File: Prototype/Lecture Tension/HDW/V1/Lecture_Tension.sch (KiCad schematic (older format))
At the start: 34 parts

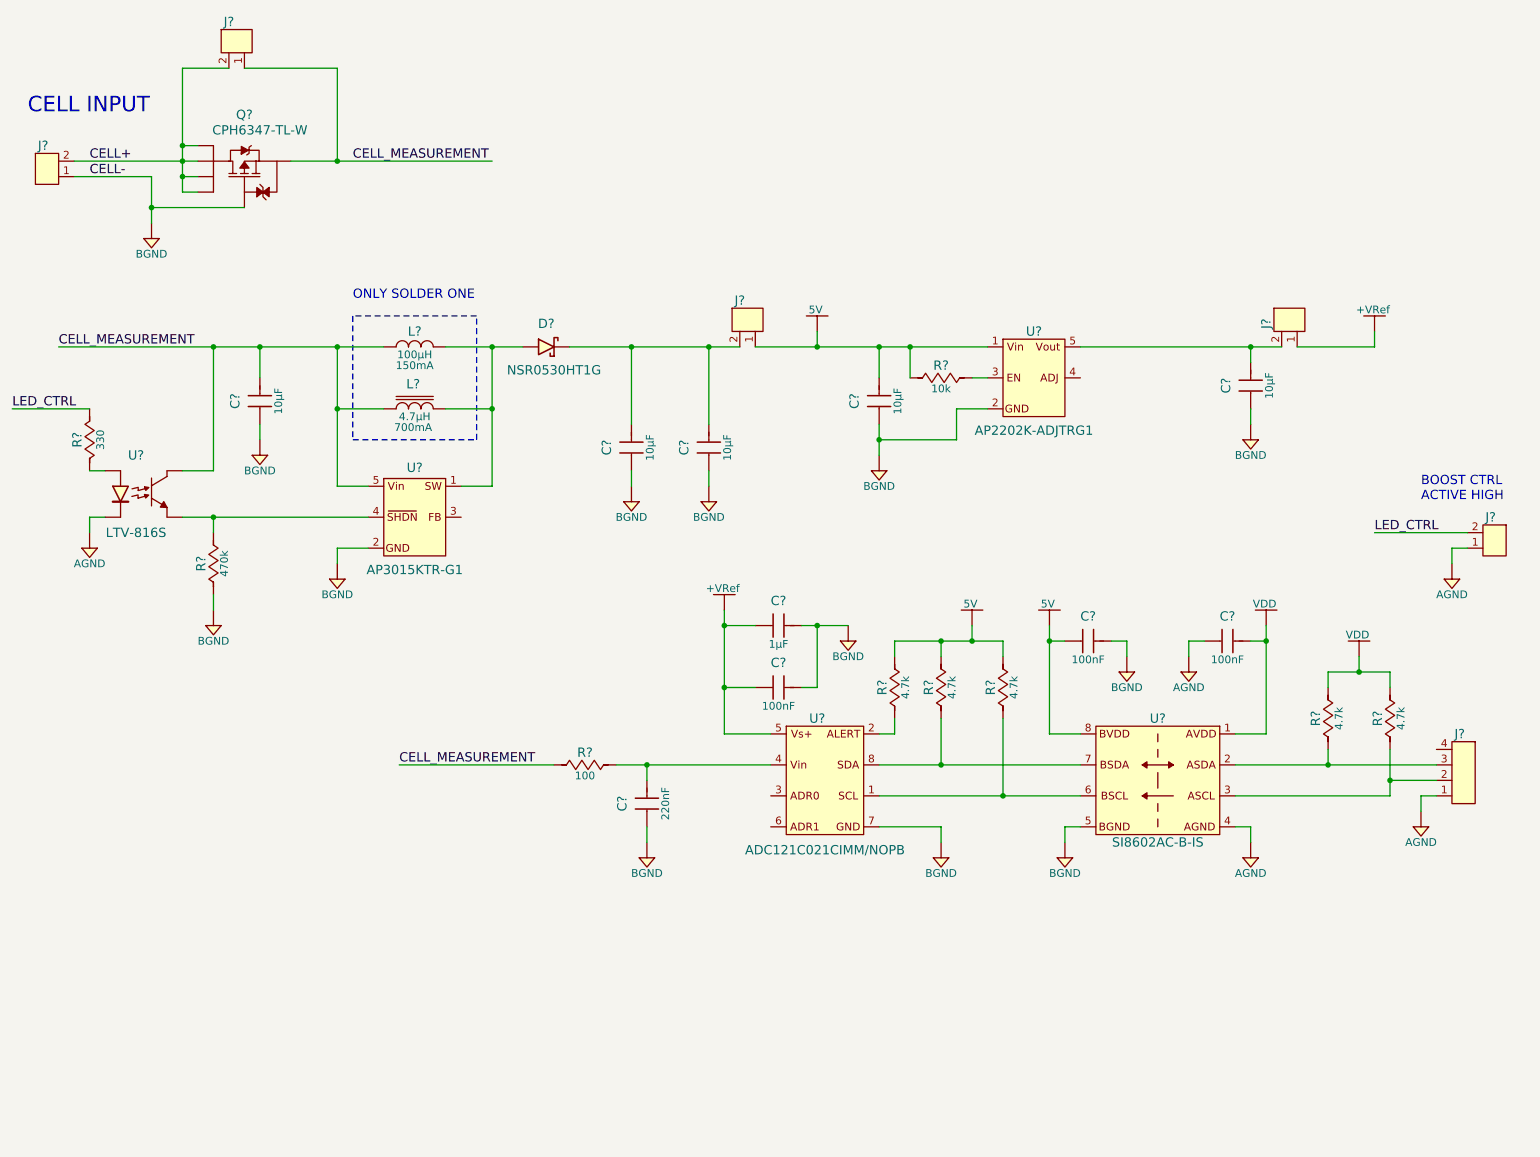
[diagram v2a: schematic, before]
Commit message: need tension divider LDO
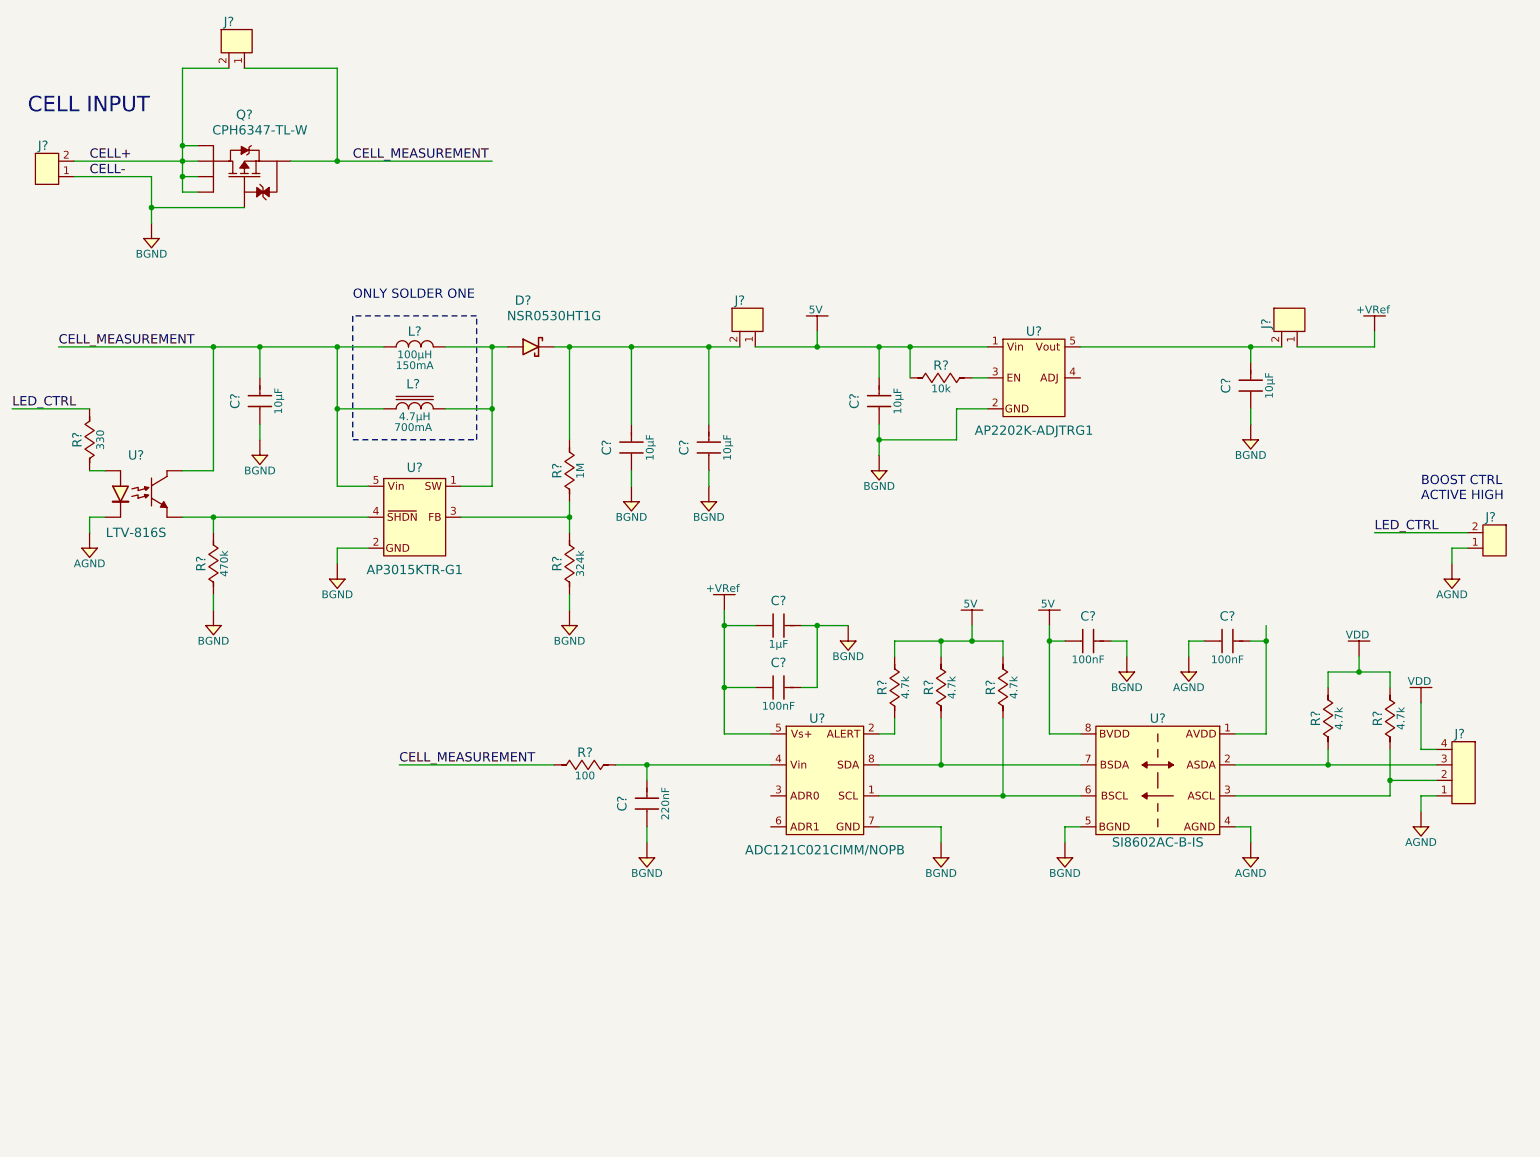
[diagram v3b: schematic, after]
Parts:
- added R?: RC0805JR-071ML, Resistors:R0805, symbol RC0805JR-071ML
- added R?: RC0805FR-07324KL, Resistors:R0805, symbol RC0805FR-07324KL
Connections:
- net BGND: now also R?.1
- net VDD: now also J?.4; no longer C?.2, U?.1 (AVDD)
- net at U?.3 (FB): now also R?.1, R?.2
- net at C?.2, C?.2, D?.1 (Cathode)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: now also R?.2
- new net: C?.2, U?.1 (AVDD)
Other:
- moved on the sheet: D?
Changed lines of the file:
@@
 L VDD #PWR?
 U 1 1 591B5717
-P 8700 4500
-F 0 "#PWR?" H 8700 4350 50  0001 C CNN
-F 1 "VDD" H 8690 4640 50  0000 C CNN
-F 2 "" H 8700 4500 60  0000 C CNN
-F 3 "" H 8700 4350 60  0000 C CNN
-	1    8700 4500
+P 9700 5000
+F 0 "#PWR?" H 9700 4850 50  0001 C CNN
+F 1 "VDD" H 9690 5140 50  0000 C CNN
+F 2 "" H 9700 5000 60  0000 C CNN
+F 3 "" H 9700 4850 60  0000 C CNN
+	1    9700 5000
 	1    0    0    -1
 $EndComp
@@
 	8600 4600 8700 4600
 Wire Wire Line
-	8700 4500 8700 4600
-Wire Wire Line
-	8700 4600 8700 5200
+	8700 4500 8700 5200
 Wire Wire Line
 	8200 4700 8200 4600
@@
 	9100 4900 9100 4800
 Wire Wire Line
-	9100 4800 9300 4800
-Wire Wire Line
-	9300 4800 9500 4800
+	9100 4800 9500 4800
 Wire Wire Line
 	9300 4800 9300 4700
 Connection ~ 9300 4800
 Wire Wire Line
-	8500 5400 9100 5400
-Wire Wire Line
-	9100 5400 9800 5400
+	8500 5400 9800 5400
 Wire Wire Line
 	9100 5400 9100 5300
@@
 	9500 4800 9500 4900
 Wire Wire Line
-	9500 5300 9500 5500
-Wire Wire Line
-	9500 5500 9500 5600
+	9500 5300 9500 5600
 Wire Wire Line
 	9500 5600 8500 5600
@@
 $EndComp
 Wire Wire Line
-	7300 4500 7300 4600
-Wire Wire Line
-	7300 4600 7300 5200
+	7300 4500 7300 5200
 Wire Wire Line
 	7300 4600 7400 4600
@@
 $EndComp
 Wire Wire Line
-	5200 4400 5200 4500
-Wire Wire Line
-	5200 4500 5200 4900
-Wire Wire Line
-	5200 4900 5200 5200
+	5200 4400 5200 5200
 Wire Wire Line
 	5200 5200 5500 5200
@@
 	5800 4900 5800 4500
 Wire Wire Line
-	5700 4500 5800 4500
-Wire Wire Line
-	5800 4500 6000 4500
+	5700 4500 6000 4500
 Connection ~ 5800 4500
 $Comp
@@
 	6600 4700 6600 4600
 Wire Wire Line
-	6300 4600 6600 4600
-Wire Wire Line
-	6600 4600 6800 4600
-Wire Wire Line
-	6800 4600 7000 4600
+	6300 4600 7000 4600
 Wire Wire Line
 	7000 4600 7000 4700
@@
 Connection ~ 6800 4600
 Wire Wire Line
-	6200 5400 6600 5400
-Wire Wire Line
-	6600 5400 7500 5400
+	6200 5400 7500 5400
 Wire Wire Line
 	6600 5400 6600 5100
@@
 	7000 5100 7000 5600
 Wire Wire Line
-	6200 5600 7000 5600
-Wire Wire Line
-	7000 5600 7500 5600
+	6200 5600 7500 5600
 Connection ~ 7000 5600
 $Comp
@@
 $EndComp
 Wire Wire Line
-	1000 1500 1700 1500
-Wire Wire Line
-	1700 1500 1800 1500
+	1000 1500 1800 1500
 Wire Wire Line
 	1000 1600 1500 1600
@@
 $EndComp
 Wire Wire Line
-	1500 1600 1500 1800
-Wire Wire Line
-	1500 1800 1500 1900
-Wire Wire Line
-	1700 900  1700 1400
-Wire Wire Line
-	1700 1400 1700 1500
-Wire Wire Line
-	1700 1500 1700 1600
-Wire Wire Line
-	1700 1600 1700 1700
+	1500 1600 1500 1900
+Wire Wire Line
+	1700 900  1700 1700
 Wire Wire Line
 	1700 1400 1800 1400
@@
 	2700 900  2700 1500
 Wire Wire Line
-	2400 1500 2700 1500
-Wire Wire Line
-	2700 1500 3700 1500
+	2400 1500 3700 1500
 Text Label 2800 1500 0    60   ~ 0
 CELL_MEASUREMENT
@@
 CELL_MEASUREMENT
 Wire Wire Line
-	4500 5400 4700 5400
-Wire Wire Line
-	4700 5400 5500 5400
+	4500 5400 5500 5400
 Wire Wire Line
 	4700 5500 4700 5400
@@
 	3000 3100 2700 3100
 Wire Wire Line
-	2700 2700 2700 3100
-Wire Wire Line
-	2700 3100 2700 3600
+	2700 2700 2700 3600
 Wire Wire Line
 	2700 3600 2900 3600
 Wire Wire Line
-	900  2700 1900 2700
-Wire Wire Line
-	1900 2700 2200 2700
-Wire Wire Line
-	2200 2700 2700 2700
-Wire Wire Line
-	2700 2700 3000 2700
+	900  2700 3000 2700
 Connection ~ 2700 3100
 Wire Wire Line
-	3400 2700 3700 2700
-Wire Wire Line
-	3700 2700 3900 2700
-Wire Wire Line
-	3700 2700 3700 3100
-Wire Wire Line
-	3700 3100 3700 3600
+	3400 2700 3800 2700
+Wire Wire Line
+	3700 2700 3700 3600
 Wire Wire Line
 	3700 3600 3500 3600
@@
 	1100 3800 1100 3900
 Wire Wire Line
-	1700 3800 1900 3800
-Wire Wire Line
-	1900 3800 2900 3800
+	1700 3800 2900 3800
 Text Label 900  2700 0    60   ~ 0
 CELL_MEASUREMENT
@@
 L NSR0530HT1G D?
 U 1 1 591BD4B8
-P 4100 2700
-F 0 "D?" H 4050 2850 60  0000 C CNN
-F 1 "NSR0530HT1G" H 4100 2550 60  0000 C CNN
-F 2 "Diodes:SOD-323" H 4080 1700 60  0001 C CNN
-F 3 "http://www.onsemi.com/pub/Collateral/NSR0530H-D.PDF" H 4080 1600 60  0001 C CNN
-F 4 "Digikey" H 4080 2200 60  0001 C CNN "Supplier"
-F 5 "NSR0530HT1GOSCT-ND" H 4080 2100 60  0001 C CNN "Supplier Part Number"
-F 6 "ON Semiconductor" H 4080 2000 60  0001 C CNN "Manufacturer"
-F 7 "NSR0530HT1G" H 4080 1900 60  0001 C CNN "Manufacturer Part Number"
-F 8 "DIODE SCHOTTKY 30V 500MA SOD323" H 4080 1800 60  0001 C CNN "Description"
-	1    4100 2700
+P 4000 2700
+F 0 "D?" H 3900 3000 60  0000 C CNN
+F 1 "NSR0530HT1G" H 4100 2900 60  0000 C CNN
+F 2 "Diodes:SOD-323" H 3980 1700 60  0001 C CNN
+F 3 "http://www.onsemi.com/pub/Collateral/NSR0530H-D.PDF" H 3980 1600 60  0001 C CNN
+F 4 "Digikey" H 3980 2200 60  0001 C CNN "Supplier"
+F 5 "NSR0530HT1GOSCT-ND" H 3980 2100 60  0001 C CNN "Supplier Part Number"
+F 6 "ON Semiconductor" H 3980 2000 60  0001 C CNN "Manufacturer"
+F 7 "NSR0530HT1G" H 3980 1900 60  0001 C CNN "Manufacturer Part Number"
+F 8 "DIODE SCHOTTKY 30V 500MA SOD323" H 3980 1800 60  0001 C CNN "Description"
+	1    4000 2700
 	1    0    0    -1
 $EndComp
 Connection ~ 3700 2700
 Wire Wire Line
-	4200 2700 4600 2700
-Wire Wire Line
-	4600 2700 5100 2700
-Wire Wire Line
-	5100 2700 5300 2700
+	4100 2700 5300 2700
 $Comp
 L 885012107014 C?
@@
 	5800 2600 5800 2700
 Wire Wire Line
-	5400 2700 5800 2700
-Wire Wire Line
-	5800 2700 6200 2700
-Wire Wire Line
-	6200 2700 6400 2700
-Wire Wire Line
-	6400 2700 6900 2700
+	5400 2700 6900 2700
 $Comp
 L 885012107014 C?
@@
 $EndComp
 Wire Wire Line
-	6200 3200 6200 3300
-Wire Wire Line
-	6200 3300 6200 3400
+	6200 3200 6200 3400
 Wire Wire Line
 	6900 3100 6700 3100
@@
 $EndComp
 Wire Wire Line
-	7500 2700 8600 2700
-Wire Wire Line
-	8600 2700 8800 2700
+	7500 2700 8800 2700
 Wire Wire Line
 	8600 2700 8600 2800
@@
 	0    -1   1    0
 $EndComp
+$Comp
+L RC0805JR-071ML R?
+U 1 1 591C2F0F
+P 4200 3500
+F 0 "R?" H 4200 3580 60  0000 C CNN
+F 1 "RC0805JR-071ML" H 4200 3200 50  0001 C CNN
+F 2 "Resistors:R0805" H 4200 2600 30  0001 C CNN
+F 3 "http://www.yageo.com/documents/recent/PYu-RC_Group_51_RoHS_L_7.pdf" H 4200 2550 30  0001 C CNN
+F 4 "Digikey" H 4200 3100 60  0001 C CNN "Supplier"
+F 5 "311-1.0MARCT-ND" H 4200 3000 60  0001 C CNN "Supplier Part Number"
+F 6 "Yageo" H 4200 2900 60  0001 C CNN "Manufacturer"
+F 7 "RC0805JR-071ML" H 4200 2800 60  0001 C CNN "Manufacturer Part Number"
+F 8 "RES SMD 1M OHM 5% 1/8W 0805" H 4200 2700 60  0001 C CNN "Description"
+F 9 "1M" H 4200 3430 50  0000 C CNN "Resistance (Ohms)"
+F 10 "±5%" H 4610 3420 50  0001 C CNN "Tolerance (%)"
+F 11 "1/8W" H 4200 3360 50  0001 C CNN "Puissance (Watts)"
+	1    4200 3500
+	0    -1   -1   0
+$EndComp
+Wire Wire Line
+	4200 3300 4200 2700
+Connection ~ 4200 2700
+Wire Wire Line
+	4200 3700 4200 3900
+Wire Wire Line
+	4200 3800 3500 3800
+$Comp
+L RC0805FR-07324KL R?
+U 1 1 591C3C0D
+P 4200 4100
+F 0 "R?" H 4200 4180 60  0000 C CNN
+F 1 "RC0805FR-07324KL" H 4200 3800 50  0001 C CNN
+F 2 "Resistors:R0805" H 4200 3200 30  0001 C CNN
+F 3 "http://www.yageo.com/documents/recent/PYu-RC_Group_51_RoHS_L_7.pdf" H 4200 3150 30  0001 C CNN
+F 4 "Digikey" H 4200 3700 60  0001 C CNN "Supplier"
+F 5 "311-324KCRCT-ND" H 4200 3600 60  0001 C CNN "Supplier Part Number"
+F 6 "Yageo" H 4200 3500 60  0001 C CNN "Manufacturer"
+F 7 "RC0805FR-07324KL" H 4200 3400 60  0001 C CNN "Manufacturer Part Number"
+F 8 "RES SMD 324K OHM 1% 1/8W 0805" H 4200 3300 60  0001 C CNN "Description"
+F 9 "324k" H 4200 4030 50  0000 C CNN "Resistance (Ohms)"
+F 10 "±1%" H 4610 4020 50  0001 C CNN "Tolerance (%)"
+F 11 "1/8W" H 4200 3960 50  0001 C CNN "Puissance (Watts)"
+	1    4200 4100
+	0    -1   -1   0
+$EndComp
+$Comp
+L BGND #PWR?
+U 1 1 591C3CA2
+P 4200 4500
+F 0 "#PWR?" H 4200 4330 50  0001 C CNN
+F 1 "BGND" H 4200 4400 50  0000 C CNN
+F 2 "" H 4200 4600 60  0000 C CNN
+F 3 "" H 4180 4410 60  0000 C CNN
+	1    4200 4500
+	1    0    0    -1
+$EndComp
+Wire Wire Line
+	4200 4300 4200 4400
+Connection ~ 4200 3800
+Wire Wire Line
+	9700 5000 9700 5300
+Wire Wire Line
+	9700 5300 9800 5300
 $EndSCHEMATC

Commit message: complete VRef regulator
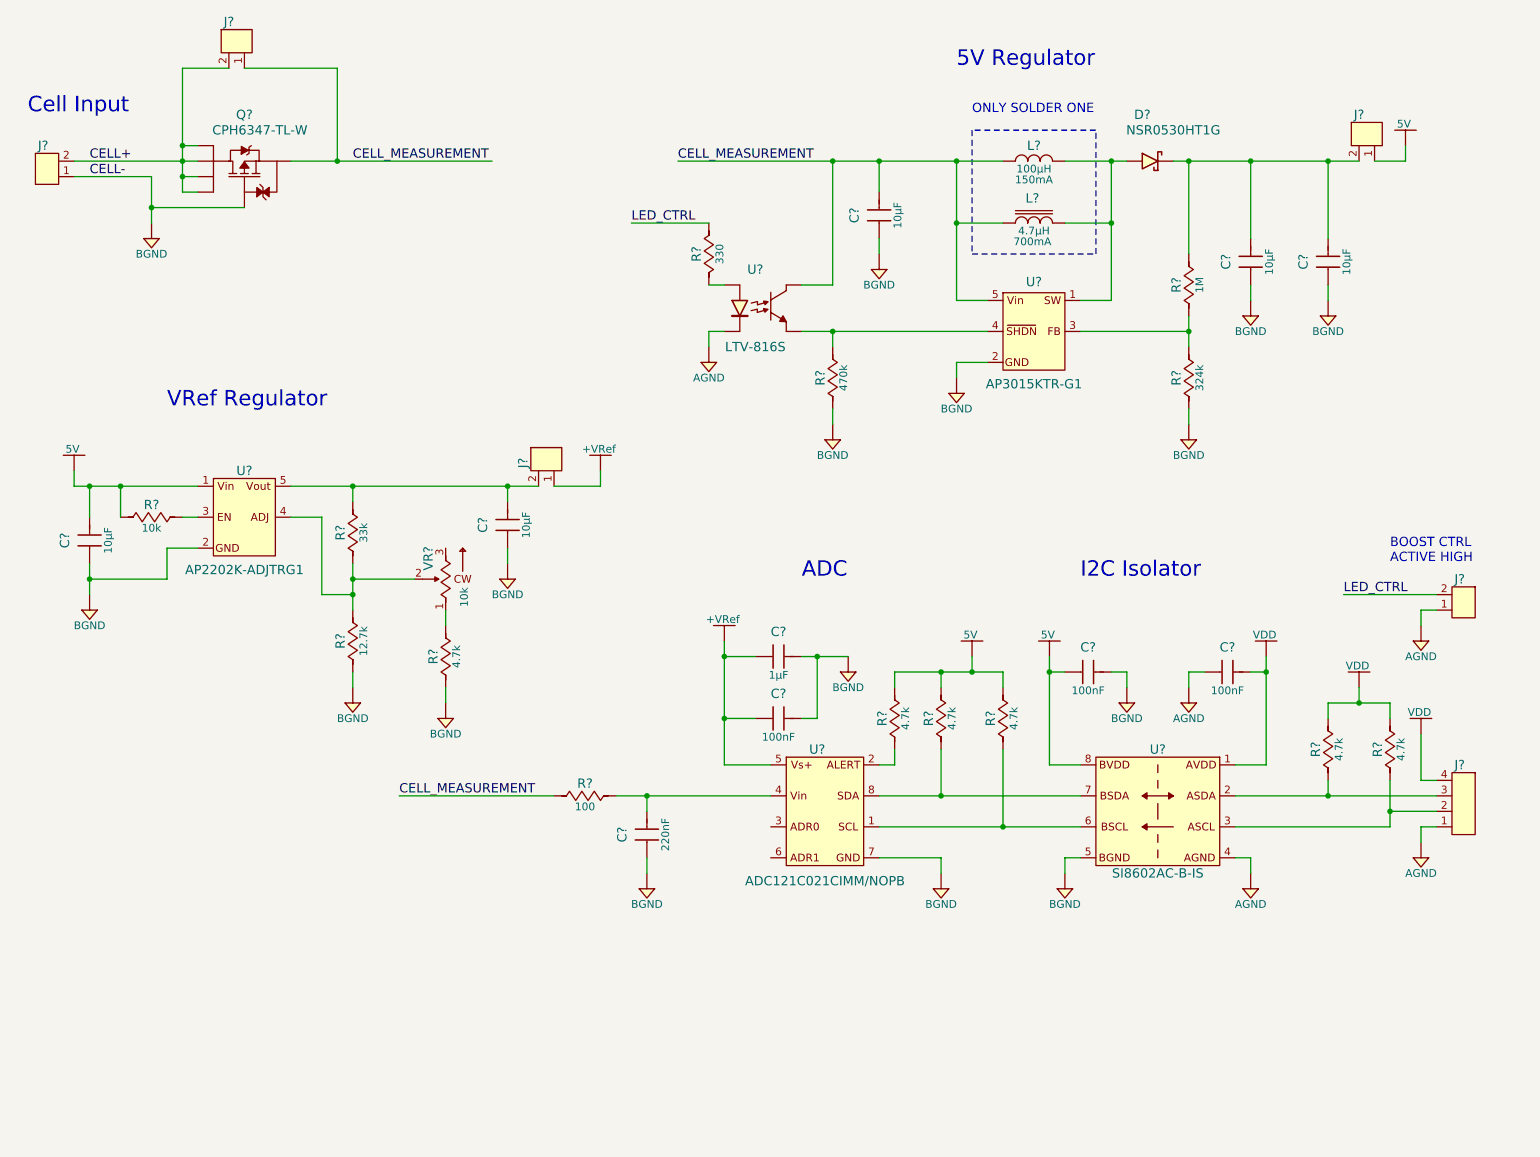
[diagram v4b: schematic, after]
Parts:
- added R?: RT0805BRD0712K7L, Resistors:R0805, symbol RT0805BRD0712K7L
- added R?: RT0805BRD0733KL, Resistors:R0805, symbol RT0805BRD0733KL
- added R?: RC0805JR-074K7L, Resistors:R0805, symbol RC0805JR-074K7L
- added VR?: CT6EP103, Resistors:CT6EP, symbol CT6EP103
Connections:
- net BGND: now also R?.1, R?.1
- net VDD: now also C?.2, U?.1 (AVDD)
- net at U?.4 (ADJ): now also R?.1, R?.2, VR?.2
- net at C?.2, J?.2, U?.5 (Vout): now also R?.2
- new net: R?.2, VR?.1
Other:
- note added: "5V Regulator"
- note added: "ADC"
- note added: "Cell Input"
- note added: "I2C Isolator"
- note added: "VRef Regulator"
- note removed: "CELL INPUT"
- moved on the sheet: C?, D?, J?, L?, R?, U?
